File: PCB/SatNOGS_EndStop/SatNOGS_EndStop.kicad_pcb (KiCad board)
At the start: 2 copper layers, 47 x 14 mm, 7 parts, among them P1 CONN_01X03, U1 TCST2103

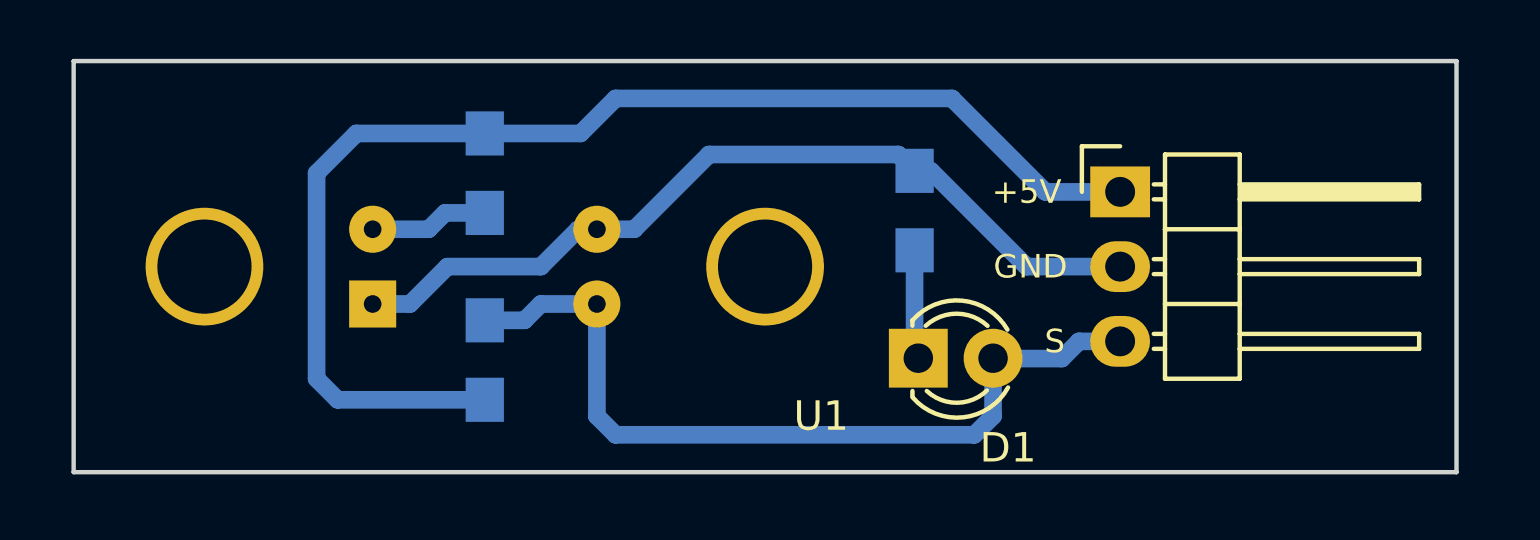
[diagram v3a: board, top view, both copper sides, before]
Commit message: Add reverse current protection to end-stop PCB.
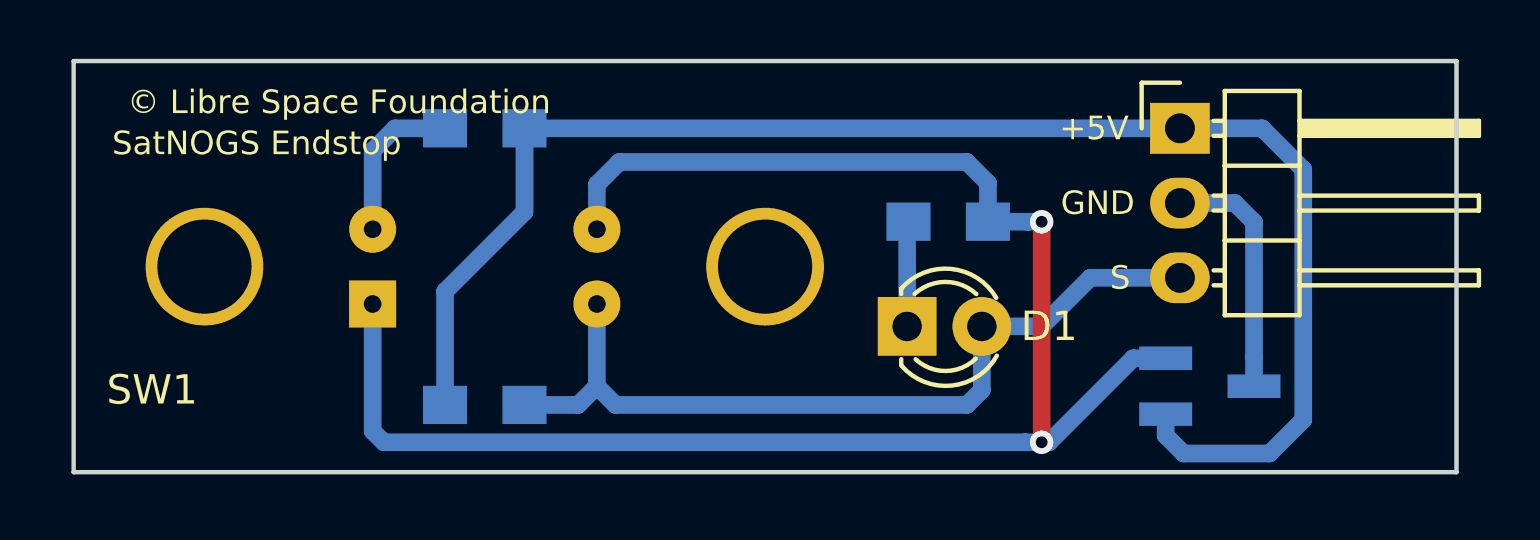
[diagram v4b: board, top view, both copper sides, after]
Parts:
- added Q1: Q_NMOS_GSD, TO_SOT_Packages_SMD:SOT-23_Handsoldering, B.Cu at (170.7, 109.5)
- moved P1 2.96 mm to (169.7, 100.7)
- moved SatNOGS Endstop 2.82 mm to (175.1, 102.2)
- moved R1 1.52 mm to (146.1, 100.7), turned to 180 degrees
- moved R2 1.52 mm to (146.1, 110.1), turned to 0 degrees
- moved R3 1.20 mm to (161.8, 103.9), turned to 0 degrees
- moved D1 1.14 mm to (160.4, 107.4)
- renumbered U1 to SW1
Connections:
- P1 pad 2: GND -> Net-(P1-Pad2)
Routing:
- net GND: track 29.1 -> 58.7 mm, vias 0 -> 2
- net +5V: track 42.7 -> 52.2 mm
- net Net-(P1-Pad2): track 0.00 -> 8.36 mm
- net Net-(R1-Pad2): track 4.04 -> 5.44 mm
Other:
- net class Default: clearance 0.1 -> 0.2; via_dia 0.6 -> 0.8
- rule trace_clearance: 0.1 -> 0.2
